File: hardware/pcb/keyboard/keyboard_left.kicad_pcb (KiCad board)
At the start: 2 copper layers, 133.8 x 110.4 mm, 113 parts, among them J1 SM03B-SRSS-TB, J2 PJ320D, J3 HRO_TYPE-C-31-M-12, J4 FH34SRJ-12S-0.5SH, SW29 PTS845, U1 74HC4051, U2 OPA350UA, U3 PRTR5V0U2X, U4 XC6220B331MR-G, U5 STM32G431KBTx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

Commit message: rev2
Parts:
- moved J1 1.00 mm to (197.0, 59.1)
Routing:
- net A5: track 23.8 -> 26.7 mm, vias 40 -> 39
- net SWDIO: track 30.9 -> 31.9 mm
- net SWCLK: track 25.6 -> 25.1 mm
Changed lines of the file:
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@@
 	(footprint "Connector_JST:JST_SH_SM03B-SRSS-TB_1x03-1MP_P1.00mm_Horizontal"
 		(layer "F.Cu")
-		(at 197.023 58.055 90)
+		(at 197.023 59.055 90)
 		(descr "JST SH series connector, SM03B-SRSS-TB (http://www.jst-mfg.com/product/pdf/eng/eSH.pdf), generated with kicad-footprint-generator")
 		(tags "connector JST SH horizontal")
@@
 	)
 	(segment
-		(start 189.05 57.981)
-		(end 189.05 66.36)
+		(start 195.023 56.472)
+		(end 193.334 54.783)
 		(width 0.25)
 		(layer "F.Cu")
@@
 	)
 	(segment
-		(start 195.023 57.055)
-		(end 193.315 55.347)
+		(start 189.05 57.981)
+		(end 189.05 66.36)
 		(width 0.25)
 		(layer "F.Cu")
@@
 	)
 	(segment
-		(start 194.775 76.872)
-		(end 193.882 76.872)
+		(start 195.023 58.055)
+		(end 195.023 56.472)
 		(width 0.25)
 		(layer "F.Cu")
@@
 	)
 	(segment
-		(start 194.973 72.283)
-		(end 194.973 76.674)
+		(start 194.775 76.872)
+		(end 193.882 76.872)
 		(width 0.25)
 		(layer "F.Cu")
@@
 	)
 	(segment
-		(start 193.315 55.347)
-		(end 193.315 54.745)
+		(start 194.973 72.283)
+		(end 194.973 76.674)
 		(width 0.25)
 		(layer "F.Cu")
@@
 	)
 	(segment
+		(start 195.023 60.055)
+		(end 193.545 60.055)
+		(width 0.25)
+		(layer "F.Cu")
+		(net 30)
+	)
+	(segment
 		(start 193.716 73.238702)
 		(end 193.714 73.240702)
@@
 	)
 	(segment
-		(start 195.023 59.055)
-		(end 194.085 59.055)
-		(width 0.25)
-		(layer "F.Cu")
-		(net 30)
-	)
-	(segment
 		(start 193.716 73.761298)
 		(end 193.716 74.638702)
@@
 	)
 	(segment
-		(start 194.085 59.055)
-		(end 193.315 59.825)
-		(width 0.25)
-		(layer "F.Cu")
-		(net 30)
-	)
-	(segment
 		(start 193.714 73.240702)
 		(end 193.714 73.759298)
@@
 	)
 	(segment
-		(start 190.05 33.97)
-		(end 190.02 33.97)
+		(start 192.507 81.166)
+		(end 191.696 80.355)
 		(width 0.25)
 		(layer "F.Cu")
@@
 	)
 	(segment
-		(start 192.507 81.166)
-		(end 191.696 80.355)
+		(start 193.315 58.121999)
+		(end 193.315 57.285)
 		(width 0.25)
 		(layer "F.Cu")
@@
 	)
 	(segment
+		(start 194.248001 59.055)
+		(end 193.315 58.121999)
+		(width 0.25)
+		(layer "F.Cu")
+		(net 61)
+	)
+	(segment
 		(start 196.129 85.715)
 		(end 196.977 84.867)
@@
 	)
 	(segment
+		(start 195.023 59.055)
+		(end 194.248001 59.055)
+		(width 0.25)
+		(layer "F.Cu")
+		(net 61)
+	)
+	(segment
 		(start 191.893 86.955)
 		(end 191.893 90.242)
@@
 		(layers "F.Cu" "B.Cu")
 		(net 61)
-	)
-	(via
-		(at 198.408 57.602)
-		(size 0.7)
-		(drill 0.4)
-		(layers "F.Cu" "B.Cu")
-		(net 61)

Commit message: init memory
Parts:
- added C14: 10n, PCM_Capacitor_SMD_AKL:C_0603_1608Metric, F.Cu at (184.7, 67.6)
- added H18: ~, ec_parts:SMT-SO-M1.6-screwhole_only, F.Cu at (182.0, 64.5)
- added H19: ~, ec_parts:SMT-SO-M1.6-screwhole_only, F.Cu at (197.8, 64.5)
- added U6: 24FC01T-I/OT, ec_parts:SOT-23-5_2P9X1P6_MCH, F.Cu at (182.4, 70.2)
- J4: value FH34SRJ-12S-0.5SH -> HRS_FH34SRJ-06S-0.5SH(50); footprint ec_parts:HRS_FH34SRJ-12S-0.5SH(50) -> ec_parts:CONN6x1_FH34SRJ-6S-0.5SH50_HIR
- moved R1 8.58 mm to (185.3, 54.2), turned to 180 degrees
- moved J4 7.84 mm to (189.8, 69.7), turned to 0 degrees
- moved R4 5.40 mm to (185.3, 56.0), turned to 0 degrees
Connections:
- J4 pad 1: unconnected-(J4-Pin_1-Pad1) -> A5
- J4 pad 2: +5V -> ACCS_4
- J4 pad 3: +5V -> ACCS_3
- J4 pad 4: unconnected-(J4-Pin_4-Pad4) -> ACCS_2
- J4 pad 6: ACCS_2 -> unconnected-(J4-Pin_6-Pad6)
- SW29 pad MP: (no net) -> unconnected-(SW29-PadMP)_1
- U5 pad 30: ACCS_6 -> I2C1_SDA
- U5 pad 31: ACCS_7 -> I2C1_SCL
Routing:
- net +5V: track 37.9 -> 18.9 mm, vias 4 -> 3
- net ACCS_6: track 10.6 -> 0.00 mm, vias 2 -> 0
- net ACCS_7: track 10.0 -> 0.00 mm
- net VBUS: track 21.5 -> 12.6 mm
- net ACCS_1: track 15.6 -> 6.91 mm
- net I2C1_SDA: track 0.00 -> 8.02 mm, vias 0 -> 2
- net ACCS_2: track 14.7 -> 6.78 mm
- net ACCS_3: track 13.9 -> 6.66 mm
- net I2C1_SCL: track 0.00 -> 6.75 mm
- net ACCS_4: track 12.9 -> 6.53 mm
- net Net-(U6-VCC): track 0.00 -> 3.80 mm
- net PB6: track 18.8 -> 21.8 mm
- net +3V3: track 113.1 -> 115.8 mm, vias 8 -> 9
- net USART_RX: track 37.6 -> 39.1 mm
- net USART_TX: track 37.2 -> 38.5 mm
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
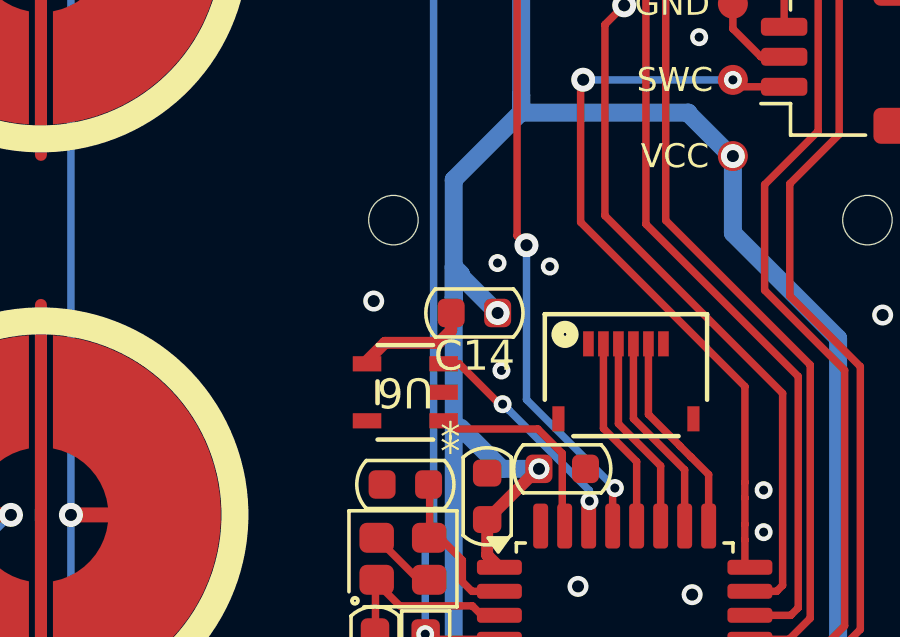
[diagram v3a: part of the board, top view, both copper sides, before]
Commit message: add pull up register for I2C.
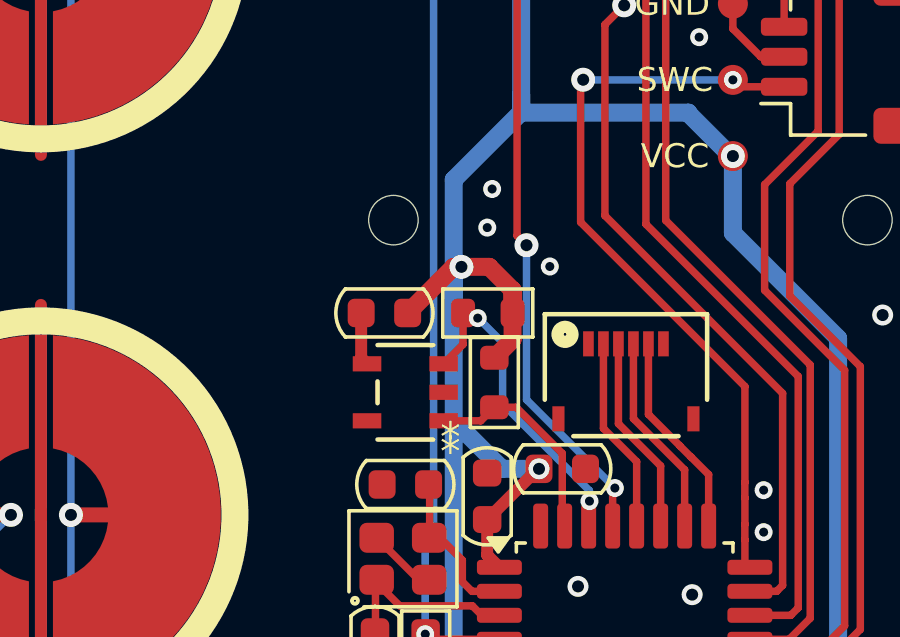
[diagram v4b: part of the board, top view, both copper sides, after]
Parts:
- added R10: 10k, PCM_Resistor_SMD_AKL:R_0603_1608Metric, F.Cu at (185.4, 69.9)
- added R9: 10k, PCM_Resistor_SMD_AKL:R_0603_1608Metric, F.Cu at (185.1, 67.6)
- moved C14 3.00 mm to (181.7, 67.6)
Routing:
- net +3V3: track 115.8 -> 121.7 mm
- net I2C1_SDA: track 8.02 -> 10.9 mm
- net Net-(U6-VCC): track 3.80 -> 1.78 mm
- net A5: vias 35 -> 34

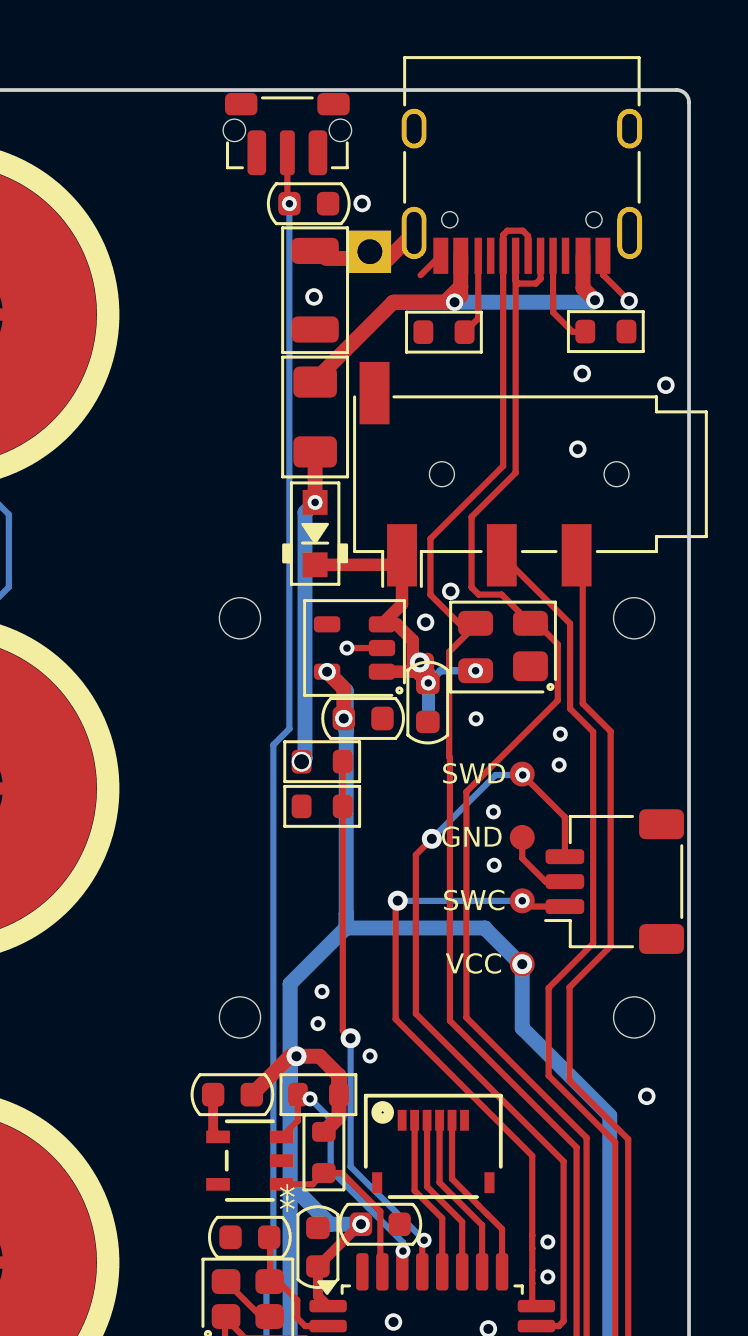
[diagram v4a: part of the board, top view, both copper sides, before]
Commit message: fix acc connection.
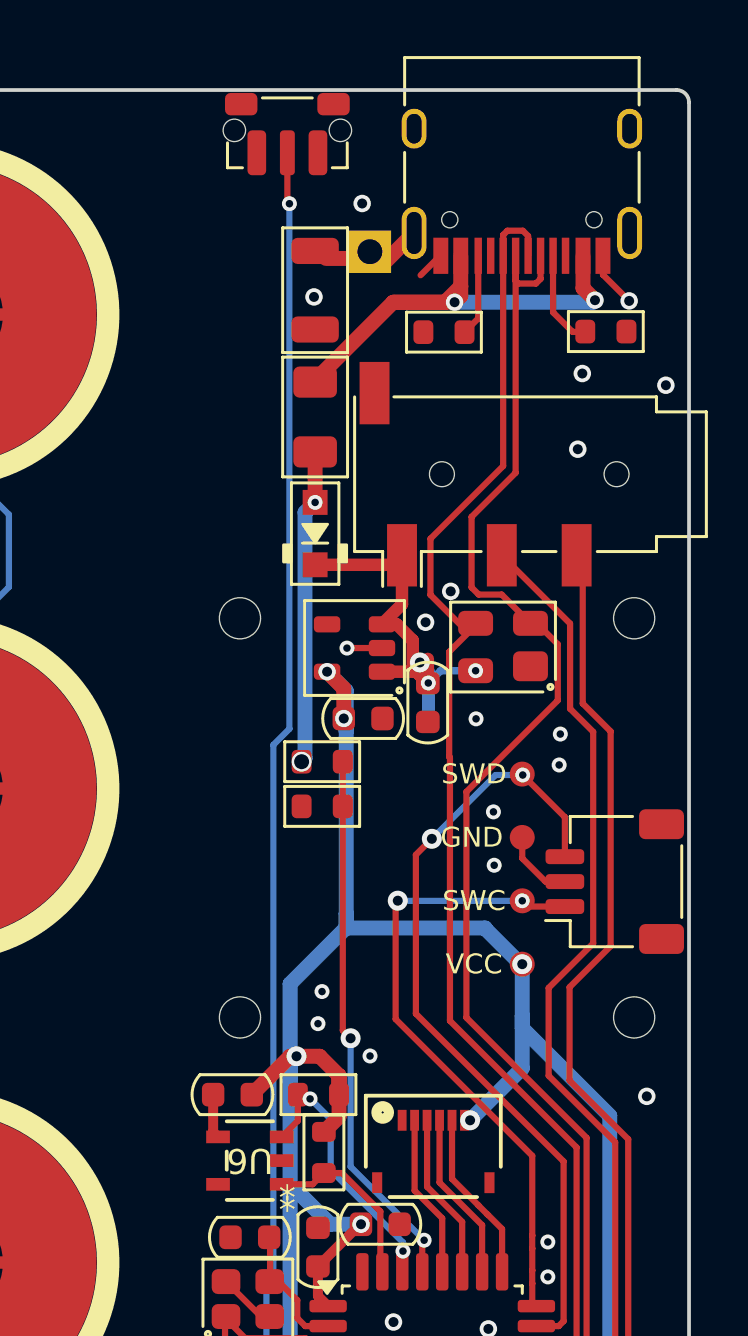
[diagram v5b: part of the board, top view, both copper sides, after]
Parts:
- removed C1: 0.1uF, PCM_Capacitor_SMD_AKL:C_0603_1608Metric
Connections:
- J4 pad 6: unconnected-(J4-Pin_6-Pad6) -> +3V3
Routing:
- net +3V3: track 121.7 -> 126.7 mm, vias 9 -> 10

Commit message: update schema.
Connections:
- net ACCS_1 renamed PA15
- net ACCS_2 renamed PB3
- net ACCS_3 renamed PB4
- net ACCS_4 renamed PB5
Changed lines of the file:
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@@
 	(net 16 "Net-(J3-CC1)")
 	(net 17 "Net-(J3-CC2)")
-	(net 18 "ACCS_1")
+	(net 18 "PA15")
 	(net 19 "SWDIO")
 	(net 20 "+5V")
@@
 	(net 40 "D+")
 	(net 41 "D-")
-	(net 42 "ACCS_2")
-	(net 43 "ACCS_3")
-	(net 44 "ACCS_4")
+	(net 42 "PB4")
+	(net 43 "PB5")
+	(net 44 "PB3")
 	(net 45 "Net-(U5-PF0)")
 	(net 46 "Net-(U5-PF1)")
@@
 			(size 0.3556 0.8382)
 			(layers "F.Cu" "F.Mask" "F.Paste")
-			(net 44 "ACCS_4")
+			(net 43 "PB5")
 			(pinfunction "Pin_2")
 			(pintype "passive")
@@
 			(size 0.3556 0.8382)
 			(layers "F.Cu" "F.Mask" "F.Paste")
-			(net 43 "ACCS_3")
+			(net 42 "PB4")
 			(pinfunction "Pin_3")
 			(pintype "passive")
@@
 			(size 0.3556 0.8382)
 			(layers "F.Cu" "F.Mask" "F.Paste")
-			(net 42 "ACCS_2")
+			(net 44 "PB3")
 			(pinfunction "Pin_4")
 			(pintype "passive")
@@
 			(size 0.3556 0.8382)
 			(layers "F.Cu" "F.Mask" "F.Paste")
-			(net 18 "ACCS_1")
+			(net 18 "PA15")
 			(pinfunction "Pin_5")
 			(pintype "passive")
@@
 			(layers "F.Cu" "F.Mask" "F.Paste")
 			(roundrect_rratio 0.25)
-			(net 18 "ACCS_1")
+			(net 18 "PA15")
 			(pinfunction "PA15")
 			(pintype "bidirectional")
@@
 			(layers "F.Cu" "F.Mask" "F.Paste")
 			(roundrect_rratio 0.25)
-			(net 42 "ACCS_2")
+			(net 44 "PB3")
 			(pinfunction "PB3")
 			(pintype "bidirectional")
@@
 			(layers "F.Cu" "F.Mask" "F.Paste")
 			(roundrect_rratio 0.25)
-			(net 43 "ACCS_3")
+			(net 42 "PB4")
 			(pinfunction "PB4")
 			(pintype "bidirectional")
@@
 			(layers "F.Cu" "F.Mask" "F.Paste")
 			(roundrect_rratio 0.25)
-			(net 44 "ACCS_4")
+			(net 43 "PB5")
 			(pinfunction "PB5")
 			(pintype "bidirectional")
@@
 	)
 	(segment
-		(start 191.707 72.824)
-		(end 191.707 74.697)
+		(start 190.907 72.693)
+		(end 190.907 74.697)
 		(width 0.25)
 		(layer "F.Cu")
@@
 	)
 	(segment
-		(start 190 68.622993)
-		(end 190 71.117)
+		(start 189.5 68.622993)
+		(end 189.5 71.286)
 		(width 0.25)
 		(layer "F.Cu")
@@
 	)
 	(segment
-		(start 190 71.117)
-		(end 191.707 72.824)
+		(start 189.5 71.286)
+		(end 190.907 72.693)
 		(width 0.25)
 		(layer "F.Cu")
@@
 	)
 	(segment
-		(start 190.907 72.693)
-		(end 190.907 74.697)
+		(start 188.999999 71.442999)
+		(end 188.999999 68.622993)
 		(width 0.25)
 		(layer "F.Cu")
@@
 	)
 	(segment
-		(start 189.5 68.622993)
-		(end 189.5 71.286)
+		(start 190.107 74.697)
+		(end 190.107 72.55)
 		(width 0.25)
 		(layer "F.Cu")
@@
 	)
 	(segment
-		(start 189.5 71.286)
-		(end 190.907 72.693)
+		(start 190.107 72.55)
+		(end 188.999999 71.442999)
 		(width 0.25)
 		(layer "F.Cu")
@@
 	)
 	(segment
-		(start 188.999999 71.442999)
-		(end 188.999999 68.622993)
+		(start 191.707 72.824)
+		(end 191.707 74.697)
 		(width 0.25)
 		(layer "F.Cu")
@@
 	)
 	(segment
-		(start 190.107 74.697)
-		(end 190.107 72.55)
+		(start 190 68.622993)
+		(end 190 71.117)
 		(width 0.25)
 		(layer "F.Cu")
@@
 	)
 	(segment
-		(start 190.107 72.55)
-		(end 188.999999 71.442999)
+		(start 190 71.117)
+		(end 191.707 72.824)
 		(width 0.25)
 		(layer "F.Cu")

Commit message: Generate production files.
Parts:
- D1: value 1N5819 -> BAT60B
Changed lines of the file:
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@@
 	(paper "A4")
 	(title_block
-		(title "Corne EEC")
-		(date "2023-07-18")
-		(rev "1.0")
-		(comment 1 "Copyright © 2023")
+		(title "Corne EEC - Keyboard Left")
+		(date "2025-09-18")
+		(rev "2.0")
 		(comment 2 "MIT License")
 	)
@@
 			)
 		)
-		(property "Value" "1N5819"
+		(property "Value" "BAT60B"
 			(at 0.1 1.9 90)
 			(layer "F.Fab")
@@
 			)
 		)
-		(property "Comment" ""
+		(property "Comment" "Alternative: 1N5819"
 			(at 0 0 0)
 			(layer "F.Fab")
@@
 			)
 		)
-		(property "Comment" ""
+		(property "Comment" "Alternative: AP2112K"
 			(at 0 0 0)
 			(layer "F.Fab")

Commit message: Rev 2.1
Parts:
- removed H18, H19: ~, ec_parts:SMT-SO-M1.6-screwhole_only
- D1: value BAT60B -> 1N5819
- J4: footprint ec_parts:CONN6x1_FH34SRJ-6S-0.5SH50_HIR -> ec_parts:CONN6x1_FH12S-6S-1SH55
- moved J4 11.0 mm to (183.8, 60.5), turned to -90 degrees
- moved TP1 5.21 mm to (197.0, 66.1)
- moved J1 5.00 mm to (197.0, 54.1)
- moved R4 3.09 mm to (184.6, 53.0), turned to -90 degrees
- moved R1 2.75 mm to (182.8, 53.0), turned to 90 degrees
- moved C9 0.18 mm to (189.5, 51.7)
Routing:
- net PA15: track 6.91 -> 21.5 mm
- net PB3: track 6.78 -> 20.4 mm
- net PB4: track 6.66 -> 19.3 mm
- net PB5: track 6.53 -> 18.1 mm
- net SWCLK: track 25.1 -> 33.4 mm, vias 2 -> 3
- net SWDIO: track 31.9 -> 36.0 mm, vias 2 -> 3
- net PB6: track 21.8 -> 25.4 mm
- net A5: track 26.7 -> 28.7 mm, vias 34 -> 31
- net D+: track 52.2 -> 50.7 mm
- net D-: track 54.8 -> 53.3 mm
- net VBUS: track 12.6 -> 11.2 mm
- net I2C1_SDA: track 10.9 -> 11.5 mm
- net USART_RX: track 39.1 -> 38.5 mm, vias 0 -> 2
- net +3V3: track 126.7 -> 126.2 mm
